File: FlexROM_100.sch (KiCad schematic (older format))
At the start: 5 parts, among them J1 LH535618 DIP LEGS, U1 28C256

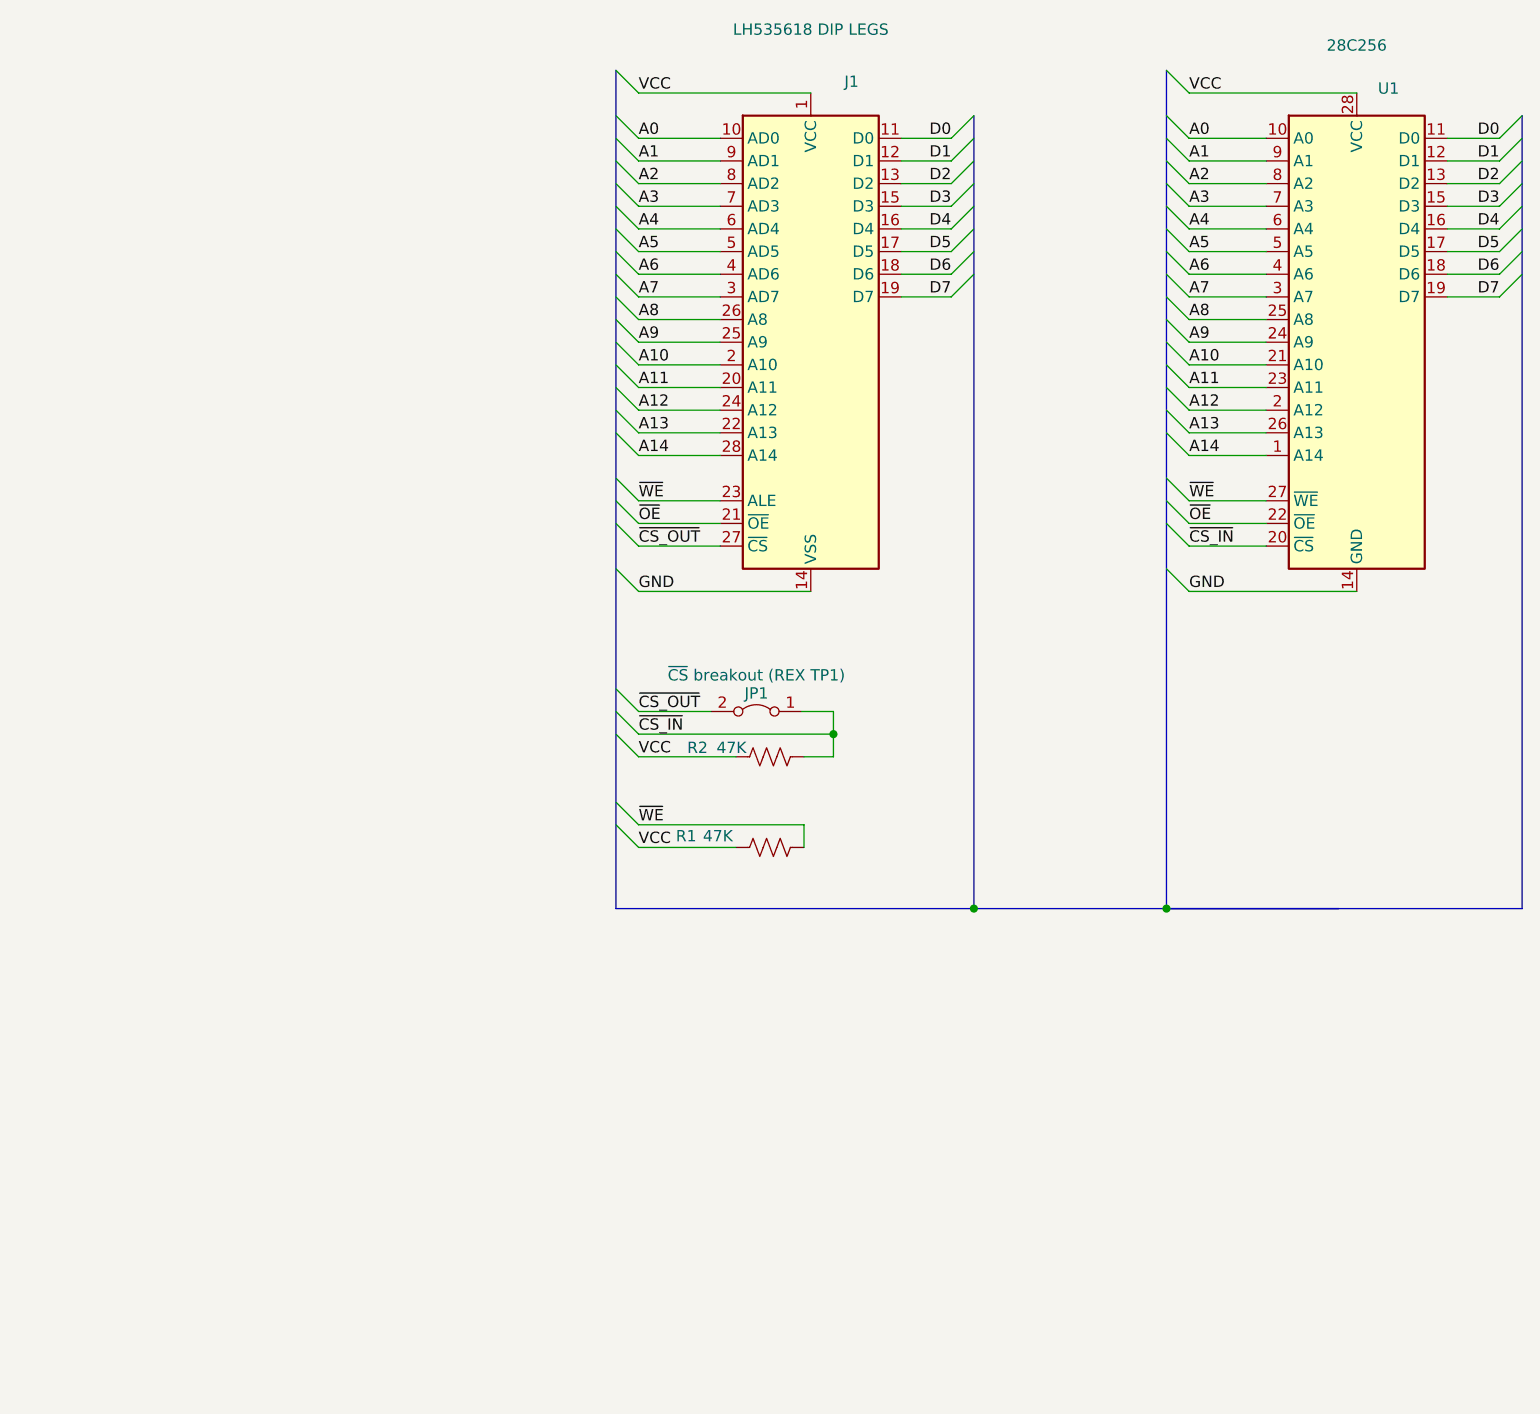
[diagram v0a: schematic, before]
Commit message: FlexROM_100 & FlashROM_100 fix ALE/WE
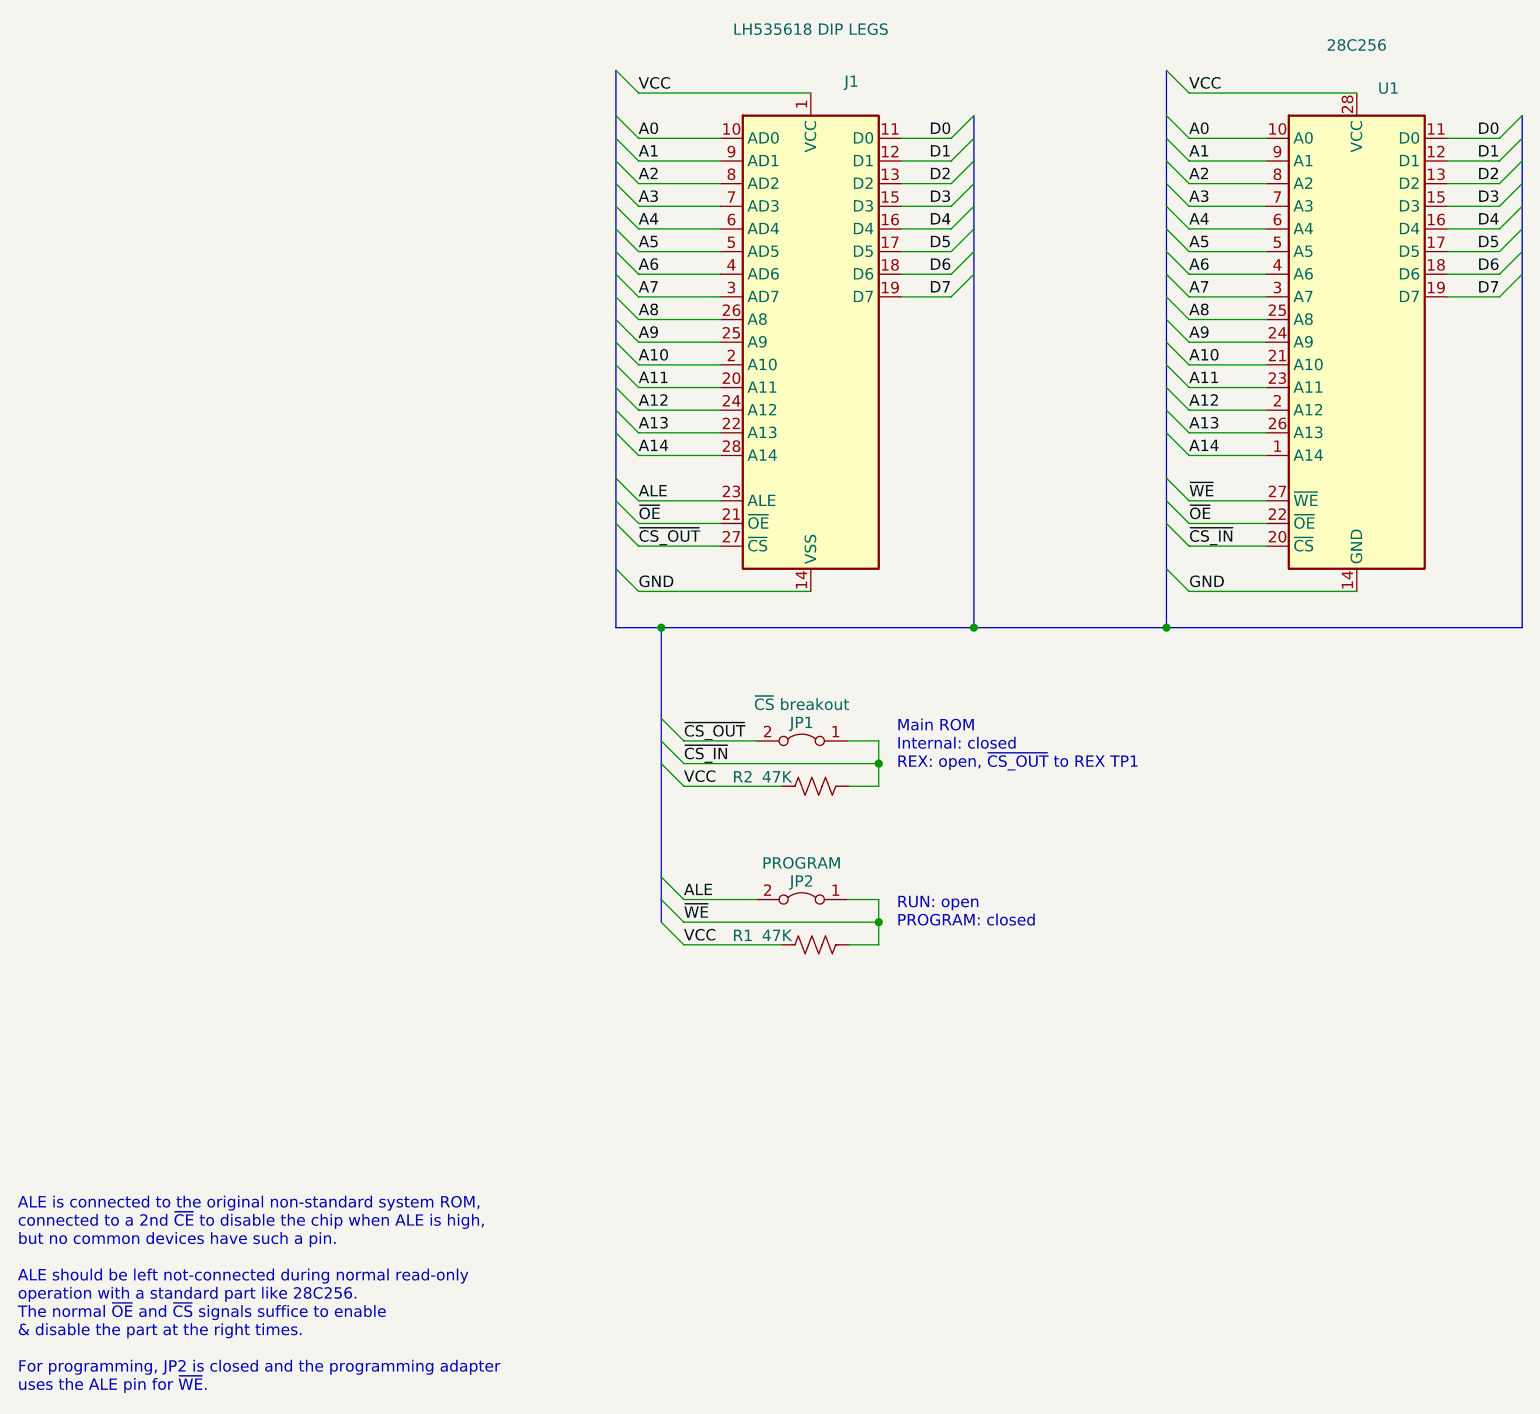
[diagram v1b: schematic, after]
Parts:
- added JP2: PROGRAM, 000_LOCAL:Pin_Header_Angled_1x02_Pitch2.54mm, symbol 000_LOCAL:Jumper_2_Bridged
- JP1: value ~CS~ breakout (REX TP1) -> ~CS~ breakout
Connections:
- net ~WE: now also JP2.1 (A); no longer J1.23 (ALE)
- new net ALE: J1.23 (ALE), JP2.2 (B)
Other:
- note added: "ALE is connected to the original non-standard system ROM,\nconnected to a 2nd ~CE~ to disable the chip when ALE is high,\nbut no common devices have such a pin.\n\nALE should be left not-connected during normal read-only\noperation with a standard part like 28C256.\nThe normal ~OE~ and ~CS~ signals suffice to enable\n& disable the part at the right times.\n\nFor programming, JP2 is closed and the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"
- note added: "Main ROM\nInternal: closed\nREX: open, ~CS_OUT~ to REX TP1\n"
- note added: "RUN: open\nPROGRAM: closed"
- moved on the sheet: JP1, R2
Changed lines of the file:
@@
 Sheet 1 1
 Title "28C256 SOIC to LH535618 DIP"
-Date ""
-Rev ""
-Comp ""
+Date "2020-11-23"
+Rev "002"
+Comp "Brian K. White - b.kenyon.w@gmail.com"
 Comment1 "TRS-80 Model 100 system rom M12"
-Comment2 "With REX main ROM support"
+Comment2 "Support REX main rom feature"
 Comment3 ""
 Comment4 ""
@@
 D7
 Entry Wire Line
-	3400 4570 3500 4670
-Entry Wire Line
-	3400 4670 3500 4770
+	3600 4700 3700 4800
+Entry Wire Line
+	3600 4800 3700 4900
 $Comp
 L 000_LOCAL:Jumper_2_Bridged JP1
 U 1 1 5E68B8A2
-P 4020 4670
-F 0 "JP1" H 4020 4750 50  0000 C CNN
-F 1 "~CS~ breakout (REX TP1)" H 4020 4830 50  0000 C CNN
-F 2 "000_LOCAL:Pin_Header_Angled_1x02_Pitch2.54mm" H 4020 4670 50  0001 C CNN
-F 3 "~" H 4020 4670 50  0001 C CNN
-	1    4020 4670
+P 4220 4800
+F 0 "JP1" H 4220 4880 50  0000 C CNN
+F 1 "~CS~ breakout" H 4220 4960 50  0000 C CNN
+F 2 "000_LOCAL:Pin_Header_Angled_1x02_Pitch2.54mm" H 4220 4800 50  0001 C CNN
+F 3 "~" H 4220 4800 50  0001 C CNN
+	1    4220 4800
 	-1   0    0    -1
 $EndComp
 Entry Wire Line
-	3400 4770 3500 4870
+	3600 4900 3700 5000
 $Comp
 L 000_LOCAL:R_US R2
 U 1 1 5E68C7F8
-P 4080 4870
-F 0 "R2" V 4040 4550 50  0000 C CNN
-F 1 "47K" V 4040 4700 50  0000 C CNN
-F 2 "000_LOCAL:R_0805" H 4080 4870 50  0001 C CNN
-F 3 "~" H 4080 4870 50  0001 C CNN
-	1    4080 4870
+P 4280 5000
+F 0 "R2" V 4240 4680 50  0000 C CNN
+F 1 "47K" V 4240 4830 50  0000 C CNN
+F 2 "000_LOCAL:R_0805" H 4280 5000 50  0001 C CNN
+F 3 "~" H 4280 5000 50  0001 C CNN
+	1    4280 5000
 	0    1    1    0
 $EndComp
 Wire Wire Line
-	3500 4670 3820 4670
-Text Label 3500 4670 0    50   ~ 0
+	3700 4800 4020 4800
+Text Label 3700 4800 0    50   ~ 0
 ~CS_OUT
 Wire Wire Line
-	3500 4870 3930 4870
-Text Label 3500 4770 0    50   ~ 0
+	3700 5000 4130 5000
+Text Label 3700 4900 0    50   ~ 0
 ~CS_IN
-Text Label 3500 4870 0    50   ~ 0
+Text Label 3700 5000 0    50   ~ 0
 VCC
-Wire Bus Line
-	3400 5540 4980 5540
-Connection ~ 5830 5540
-Wire Bus Line
-	5830 5540 7400 5540
-Entry Wire Line
-	3400 5070 3500 5170
-Entry Wire Line
-	3400 5170 3500 5270
+Wire Wire Line
+	3500 1940 4260 1940
+Wire Wire Line
+	3500 2140 3860 2140
+Wire Wire Line
+	3500 2240 3860 2240
+Wire Wire Line
+	3500 2340 3860 2340
+Wire Wire Line
+	3500 2440 3860 2440
+Wire Wire Line
+	3500 2540 3860 2540
+Wire Wire Line
+	3500 2640 3860 2640
+Wire Wire Line
+	3500 2740 3860 2740
+Wire Wire Line
+	3500 2840 3860 2840
+Wire Wire Line
+	3500 2940 3860 2940
+Wire Wire Line
+	3500 3040 3860 3040
+Wire Wire Line
+	3500 3140 3860 3140
+Wire Wire Line
+	3500 3240 3860 3240
+Wire Wire Line
+	3500 3340 3860 3340
+Wire Wire Line
+	3500 3440 3860 3440
+Wire Wire Line
+	3500 3540 3860 3540
+Wire Wire Line
+	3500 3840 3860 3840
+Wire Wire Line
+	3500 3940 3860 3940
+Wire Wire Line
+	3500 4140 4260 4140
+Wire Wire Line
+	4660 2140 4880 2140
+Wire Wire Line
+	4660 2240 4880 2240
+Wire Wire Line
+	4660 2340 4880 2340
+Wire Wire Line
+	4660 2440 4880 2440
+Wire Wire Line
+	4660 2540 4880 2540
+Wire Wire Line
+	4660 2640 4880 2640
+Wire Wire Line
+	4660 2740 4880 2740
+Wire Wire Line
+	4660 2840 4880 2840
+Wire Wire Line
+	5930 1940 6670 1940
+Wire Wire Line
+	5930 2140 6270 2140
+Wire Wire Line
+	5930 2240 6270 2240
+Wire Wire Line
+	5930 2340 6270 2340
+Wire Wire Line
+	5930 2440 6270 2440
+Wire Wire Line
+	5930 2540 6270 2540
+Wire Wire Line
+	5930 2640 6270 2640
+Wire Wire Line
+	5930 2740 6270 2740
+Wire Wire Line
+	5930 2840 6270 2840
+Wire Wire Line
+	5930 2940 6270 2940
+Wire Wire Line
+	5930 3040 6270 3040
+Wire Wire Line
+	5930 3140 6270 3140
+Wire Wire Line
+	5930 3240 6270 3240
+Wire Wire Line
+	5930 3340 6270 3340
+Wire Wire Line
+	5930 3440 6270 3440
+Wire Wire Line
+	5930 3540 6270 3540
+Wire Wire Line
+	5930 3740 6270 3740
+Wire Wire Line
+	5930 3840 6270 3840
+Wire Wire Line
+	5930 3940 6270 3940
+Wire Wire Line
+	5930 4140 6670 4140
+Wire Wire Line
+	7070 2140 7300 2140
+Wire Wire Line
+	7070 2240 7300 2240
+Wire Wire Line
+	7070 2340 7300 2340
+Wire Wire Line
+	7070 2440 7300 2440
+Wire Wire Line
+	7070 2540 7300 2540
+Wire Wire Line
+	7070 2640 7300 2640
+Wire Wire Line
+	7070 2740 7300 2740
+Wire Wire Line
+	7070 2840 7300 2840
+Wire Wire Line
+	4560 4800 4560 4900
+Wire Wire Line
+	4430 5000 4560 5000
+Wire Wire Line
+	3700 4900 4560 4900
+Connection ~ 4560 4900
+Wire Wire Line
+	4560 4900 4560 5000
+Wire Wire Line
+	4560 4800 4420 4800
+Entry Wire Line
+	3400 3640 3500 3740
+Wire Wire Line
+	3500 3740 3860 3740
+Connection ~ 4980 4300
+Wire Bus Line
+	4980 4300 5830 4300
+Connection ~ 5830 4300
+Wire Bus Line
+	5830 4300 7400 4300
+Entry Wire Line
+	3600 5400 3700 5500
+Entry Wire Line
+	3600 5500 3700 5600
+$Comp
+L 000_LOCAL:Jumper_2_Bridged JP2
+U 1 1 5FBFB30E
+P 4220 5500
+F 0 "JP2" H 4220 5580 50  0000 C CNN
+F 1 "PROGRAM" H 4220 5660 50  0000 C CNN
+F 2 "000_LOCAL:Pin_Header_Angled_1x02_Pitch2.54mm" H 4220 5500 50  0001 C CNN
+F 3 "~" H 4220 5500 50  0001 C CNN
+	1    4220 5500
+	-1   0    0    -1
+$EndComp
+Entry Wire Line
+	3600 5600 3700 5700
 $Comp
 L 000_LOCAL:R_US R1
-U 1 1 5E6B3AF8
-P 4080 5270
-F 0 "R1" V 4030 4900 50  0000 C CNN
-F 1 "47K" V 4030 5040 50  0000 C CNN
-F 2 "000_LOCAL:R_0805" H 4080 5270 50  0001 C CNN
-F 3 "~" H 4080 5270 50  0001 C CNN
-	1    4080 5270
+U 1 1 5FBFB319
+P 4280 5700
+F 0 "R1" V 4240 5380 50  0000 C CNN
+F 1 "47K" V 4240 5530 50  0000 C CNN
+F 2 "000_LOCAL:R_0805" H 4280 5700 50  0001 C CNN
+F 3 "~" H 4280 5700 50  0001 C CNN
+	1    4280 5700
 	0    1    1    0
 $EndComp
 Wire Wire Line
-	3500 5270 3930 5270
-Wire Wire Line
-	4230 5270 4230 5170
-Text Label 3500 5270 0    50   ~ 0
+	3700 5500 4020 5500
+Wire Wire Line
+	3700 5700 4130 5700
+Text Label 3700 5600 0    50   ~ 0
+~WE
+Text Label 3700 5700 0    50   ~ 0
 VCC
-Text Label 3500 5170 0    50   ~ 0
-~WE
-Connection ~ 4980 5540
-Wire Bus Line
-	4980 5540 5830 5540
-Wire Bus Line
-	5830 5540 6590 5540
-Wire Wire Line
-	3500 1940 4260 1940
-Wire Wire Line
-	3500 2140 3860 2140
-Wire Wire Line
-	3500 2240 3860 2240
-Wire Wire Line
-	3500 2340 3860 2340
-Wire Wire Line
-	3500 2440 3860 2440
-Wire Wire Line
-	3500 2540 3860 2540
-Wire Wire Line
-	3500 2640 3860 2640
-Wire Wire Line
-	3500 2740 3860 2740
-Wire Wire Line
-	3500 2840 3860 2840
-Wire Wire Line
-	3500 2940 3860 2940
-Wire Wire Line
-	3500 3040 3860 3040
-Wire Wire Line
-	3500 3140 3860 3140
-Wire Wire Line
-	3500 3240 3860 3240
-Wire Wire Line
-	3500 3340 3860 3340
-Wire Wire Line
-	3500 3440 3860 3440
-Wire Wire Line
-	3500 3540 3860 3540
-Wire Wire Line
-	3500 3840 3860 3840
-Wire Wire Line
-	3500 3940 3860 3940
-Wire Wire Line
-	3500 4140 4260 4140
-Wire Wire Line
-	4660 2140 4880 2140
-Wire Wire Line
-	4660 2240 4880 2240
-Wire Wire Line
-	4660 2340 4880 2340
-Wire Wire Line
-	4660 2440 4880 2440
-Wire Wire Line
-	4660 2540 4880 2540
-Wire Wire Line
-	4660 2640 4880 2640
-Wire Wire Line
-	4660 2740 4880 2740
-Wire Wire Line
-	4660 2840 4880 2840
-Wire Wire Line
-	5930 1940 6670 1940
-Wire Wire Line
-	5930 2140 6270 2140
-Wire Wire Line
-	5930 2240 6270 2240
-Wire Wire Line
-	5930 2340 6270 2340
-Wire Wire Line
-	5930 2440 6270 2440
-Wire Wire Line
-	5930 2540 6270 2540
-Wire Wire Line
-	5930 2640 6270 2640
-Wire Wire Line
-	5930 2740 6270 2740
-Wire Wire Line
-	5930 2840 6270 2840
-Wire Wire Line
-	5930 2940 6270 2940
-Wire Wire Line
-	5930 3040 6270 3040
-Wire Wire Line
-	5930 3140 6270 3140
-Wire Wire Line
-	5930 3240 6270 3240
-Wire Wire Line
-	5930 3340 6270 3340
-Wire Wire Line
-	5930 3440 6270 3440
-Wire Wire Line
-	5930 3540 6270 3540
-Wire Wire Line
-	5930 3740 6270 3740
-Wire Wire Line
-	5930 3840 6270 3840
-Wire Wire Line
-	5930 3940 6270 3940
-Wire Wire Line
-	5930 4140 6670 4140
-Wire Wire Line
-	7070 2140 7300 2140
-Wire Wire Line
-	7070 2240 7300 2240
-Wire Wire Line
-	7070 2340 7300 2340
-Wire Wire Line
-	7070 2440 7300 2440
-Wire Wire Line
-	7070 2540 7300 2540
-Wire Wire Line
-	7070 2640 7300 2640
-Wire Wire Line
-	7070 2740 7300 2740
-Wire Wire Line
-	7070 2840 7300 2840
-Wire Wire Line
-	4360 4670 4360 4770
-Wire Wire Line
-	4230 4870 4360 4870
-Wire Wire Line
-	3500 4770 4360 4770
-Connection ~ 4360 4770
-Wire Wire Line
-	4360 4770 4360 4870
-Wire Wire Line
-	4360 4670 4220 4670
-Wire Wire Line
-	3500 5170 4230 5170
-Entry Wire Line
-	3400 3640 3500 3740
-Wire Wire Line
-	3500 3740 3860 3740
-Wire Bus Line
-	4980 2040 4980 5540
-Wire Bus Line
-	7400 2040 7400 5540
-Wire Bus Line
-	5830 1840 5830 5540
-Wire Bus Line
-	3400 1840 3400 5540
+Wire Wire Line
+	4560 5500 4560 5600
+Wire Wire Line
+	4430 5700 4560 5700
+Wire Wire Line
+	3700 5600 4560 5600
+Connection ~ 4560 5600
+Wire Wire Line
+	4560 5600 4560 5700
+Wire Wire Line
+	4560 5500 4420 5500
+Wire Bus Line
+	3400 4300 3600 4300
+Connection ~ 3600 4300
+Wire Bus Line
+	3600 4300 4980 4300
+Text Notes 4640 5630 0    50   ~ 0
+RUN: open\nPROGRAM: closed
+Text Notes 4640 4930 0    50   ~ 0
+Main ROM\nInternal: closed\nREX: open, ~CS_OUT~ to REX TP1\n
+Text Notes 760  7680 0    50   ~ 0
+ALE is connected to the original non-standard system ROM,\nconnected to a 2nd ~CE~ to disable the chip when ALE is high,\nbut no common devices have such a pin.\n\nALE should be left not-connected during normal read-only\noperation with a standard part like 28C256.\nThe normal ~OE~ and ~CS~ signals suffice to enable\n& disable the part at the right times.\n\nFor programming, JP2 is closed and the programming adapter\nuses the ALE pin for ~WE~.
+Text Label 3700 5500 0    50   ~ 0
+ALE
 Text Label 3500 3740 0    50   ~ 0
-~WE
+ALE
+Wire Bus Line
+	3600 4300 3600 5600
+Wire Bus Line
+	7400 2040 7400 4300
+Wire Bus Line
+	4980 2040 4980 4300
+Wire Bus Line
+	3400 1840 3400 4300
+Wire Bus Line
+	5830 1840 5830 4300
 $EndSCHEMATC

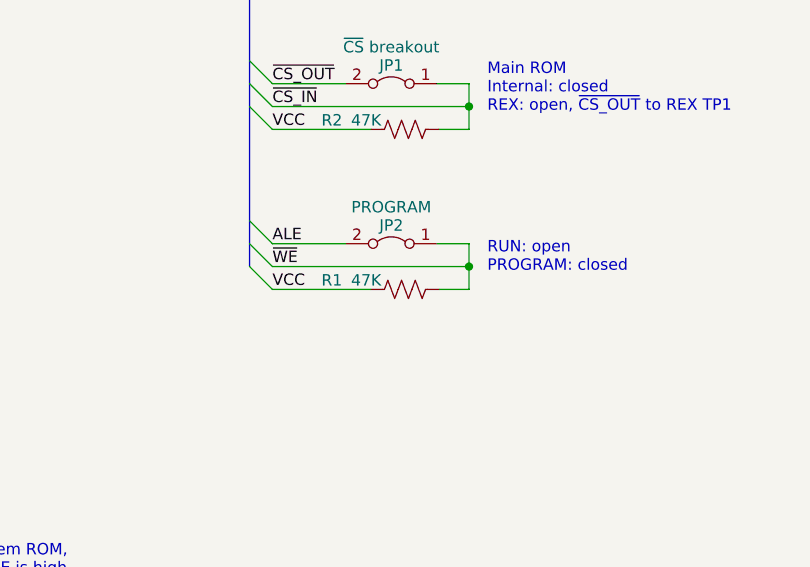
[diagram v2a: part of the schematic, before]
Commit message: add model 100 optrom programming adapter. readme and renders
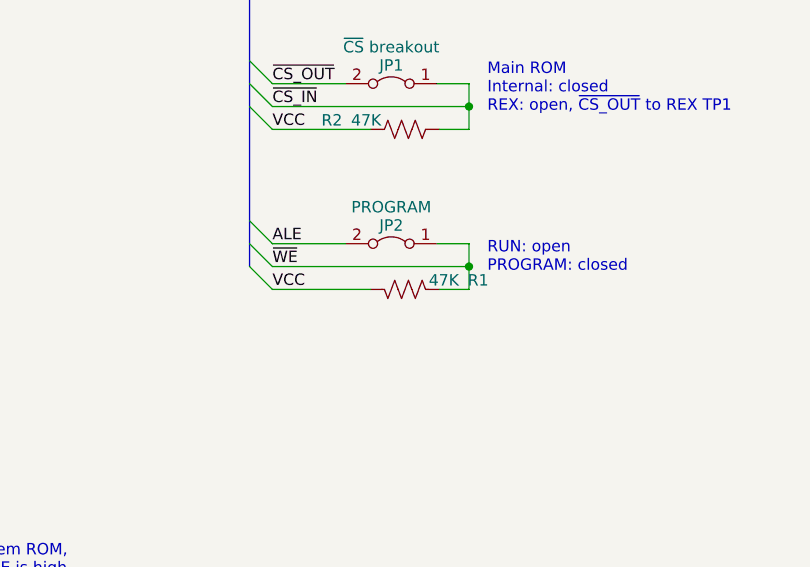
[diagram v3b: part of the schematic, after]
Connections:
- net VCC: now also R1.1; no longer R1.2
- net ~WE: now also R1.2; no longer R1.1
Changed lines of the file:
@@
 F 3 "~" H 4280 5700 50  0001 C CNN
 	1    4280 5700
-	0    1    1    0
+	0    -1   1    0
 $EndComp
 Wire Wire Line
